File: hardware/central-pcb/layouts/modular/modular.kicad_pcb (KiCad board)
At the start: 2 copper layers, 18 parts

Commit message: fix(central): resolve GPIO19/20 USB-JTAG conflict and align firmware pin mappings (H-01, FC-01)
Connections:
- J3 pad 10: GPIO17 -> 3-1
- J3 pad 11: GPIO18 -> (no net)
- J4 pad 20: 3-2 -> GPIO20
- J4 pad 21: 3-1 -> GPIO19
- J8 pad 3: 3-2 -> (no net)
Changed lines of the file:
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@@
 	(net 2 "anode")
 	(net 3 "1-2")
-	(net 4 "GPIO17")
-	(net 5 "GPIO18")
 	(net 6 "12")
 	(net 7 "13")
@@
 	(net 28 "18")
 	(net 29 "2-2")
-	(net 30 "3-2")
+	(net 30 "GPIO20")
 	(net 31 "esp32.right_header-3")
 	(net 32 "esp32.right_header-4")
@@
 	(net 38 "5")
 	(net 39 "2-3")
-	(net 40 "3-1")
+	(net 40 "GPIO19")
 	(net 41 "4-1")
 	(net 42 "5-1")
@@
 	(net 46 "anode-2")
 	(net 47 "v_out")
+	(net 48 "3-2")
+	(net 49 "3-1")
 	(footprint "central-pcb:TerminalBlock_Phoenix_MPT-0,5-2-2.54_1x02_P2.54mm_Horizontal"
 		(layer "F.Cu")
@@
 			(layers "*.Cu" "*.Mask")
 			(remove_unused_layers no)
-			(net 4 "GPIO17")
+			(net 49 "3-1")
 		)
 		(pad "11" thru_hole circle
@@
 			(layers "*.Cu" "*.Mask")
 			(remove_unused_layers no)
-			(net 5 "GPIO18")
+			(net 0 "")
 		)
 		(pad "12" thru_hole circle
@@
 			(layers "*.Cu" "*.Mask")
 			(remove_unused_layers no)
-			(net 30 "3-2")
+			(net 30 "GPIO20")
 		)
 		(pad "21" thru_hole circle
@@
 			(layers "*.Cu" "*.Mask")
 			(remove_unused_layers no)
-			(net 40 "3-1")
+			(net 40 "GPIO19")
 		)
 		(pad "22" thru_hole circle
@@
 			(layers "*.Cu" "*.Mask")
 			(remove_unused_layers no)
-			(net 40 "3-1")
+			(net 49 "3-1")
 		)
 		(pad "4" thru_hole circle
@@
 			(layers "*.Cu" "*.Mask")
 			(remove_unused_layers no)
-			(net 30 "3-2")
+			(net 0 "")
 		)
 		(pad "4" thru_hole circle

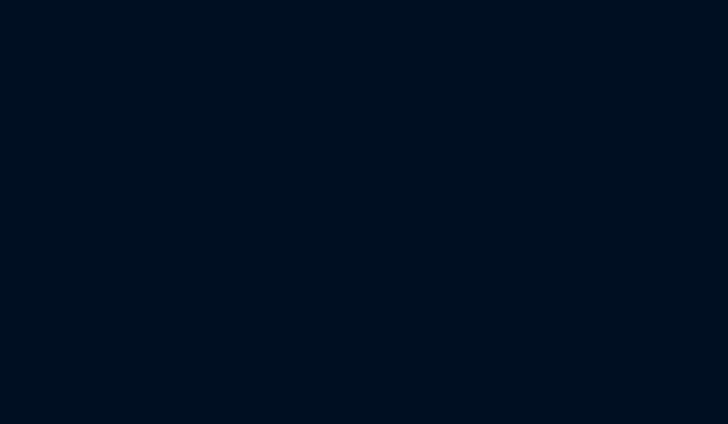
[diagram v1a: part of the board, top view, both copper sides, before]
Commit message: fix(central): correct battery telemetry divider ratio, use analogReadMilliVolts and add Zener protection (FC-03, H-07)
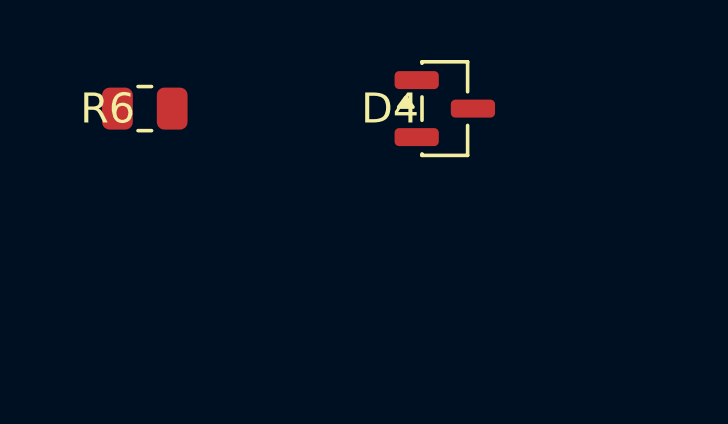
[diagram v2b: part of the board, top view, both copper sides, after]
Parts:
- added D4: , central-pcb:SOT-23, F.Cu at (10.0, 0.00)
- added R6: , central-pcb:R_0805_2012Metric, F.Cu at (0.00, 0.00)
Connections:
- C1 pad 1: v_out -> voltage_sensor-1
- J3 pad 11: (no net) -> 3-2
- J8 pad 3: (no net) -> 3-2
- R4 pad 2: v_out -> voltage_sensor-1
- R5 pad 1: v_out -> voltage_sensor-1

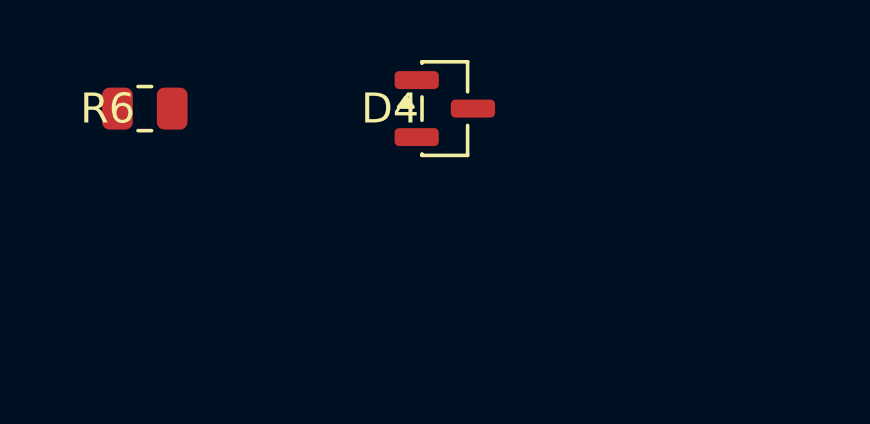
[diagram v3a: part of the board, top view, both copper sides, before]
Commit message: feat(hardware): update central PCB layout and Atopile definitions
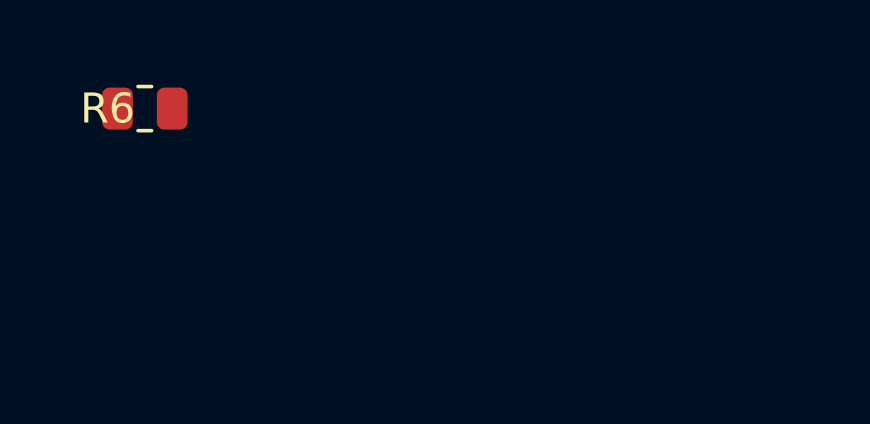
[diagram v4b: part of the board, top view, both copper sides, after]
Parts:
- removed D4: , central-pcb:SOT-23
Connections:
- net GPIO20 renamed 20
- J3 pad 21: 21 -> v_mcu_5v
- J4 pad 1: v_mcu_5v -> 2
- J4 pad 18: 18 -> 2-2
- J4 pad 19: 2-2 -> 19
- J4 pad 2: 2 -> esp32.right_header-2
- J4 pad 21: GPIO19 -> 2
- J4 pad 4: esp32.right_header-4 -> v_out
- J4 pad 5: v_out -> 1
- J4 pad 6: 1 -> 6

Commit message: feat(hardware): implement automated KiCad 3D PCB rendering and STEP CAD export
- Add headless PCB rendering script (hardware/central-pcb/scripts/render_pcb.py) supporting both native kicad-cli and Flatpak org.kicad.KiCad.
- Add clean Edge.Cuts board outline and 4x M3 corner mounting holes to profet and modular PCB layouts.
- Fix series resistor coordinates (R35 and R6) from unplaced origin (0,0) to analog divider cluster at (234,160).
- Generate high-resolution 1440p raytraced 3D isometric and orthographic renders, silkscreen vector graphics, and 3D STEP models.
- Create engineering reference guide (.agents/skills/schematic-design/references/pcb_rendering_and_visualization.md) and link in SKILL.md and docs/README.md.
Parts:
- moved R6 283.5 mm to (234.0, 160.0)
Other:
- board outline added: 274 x 154 mm
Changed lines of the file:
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@@
 	(footprint "central-pcb:R_0805_2012Metric"
 		(layer "F.Cu")
-		(at 0 0 0)
+		(at 234 160 0)
 		(descr "Resistor SMD 0805 (2012 Metric), square (rectangular) end terminal, IPC-7351 nominal, (Body size source: IPC-SM-782 page 72, https://www.pcb-3d.com/wordpress/wp-content/uploads/ipc-sm-782a_amendment_1_and_2.pdf)")
 		(tags "resistor")
@@
 		)
 	)
+	(gr_circle
+		(center 24 24)
+		(end 25.6 24)
+		(stroke
+			(width 0.15)
+			(type solid)
+		)
+		(fill none)
+		(layer "Edge.Cuts")
+		(uuid "00000000-edge-cuts-hole-000000000001")
+	)
+	(gr_circle
+		(center 286 24)
+		(end 287.6 24)
+		(stroke
+			(width 0.15)
+			(type solid)
+		)
+		(fill none)
+		(layer "Edge.Cuts")
+		(uuid "00000000-edge-cuts-hole-000000000002")
+	)
+	(gr_circle
+		(center 24 166)
+		(end 25.6 166)
+		(stroke
+			(width 0.15)
+			(type solid)
+		)
+		(fill none)
+		(layer "Edge.Cuts")
+		(uuid "00000000-edge-cuts-hole-000000000003")
+	)
+	(gr_circle
+		(center 286 166)
+		(end 287.6 166)
+		(stroke
+			(width 0.15)
+			(type solid)
+		)
+		(fill none)
+		(layer "Edge.Cuts")
+		(uuid "00000000-edge-cuts-hole-000000000004")
+	)
+	(gr_rect
+		(start 18 18)
+		(end 292 172)
+		(stroke
+			(width 0.15)
+			(type solid)
+		)
+		(fill none)
+		(layer "Edge.Cuts")
+		(uuid "00000000-edge-cuts-rect-000000000001")
+	)
 )
